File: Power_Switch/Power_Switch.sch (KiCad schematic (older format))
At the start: 13 parts, among them J1 CONN_01X04_MALE, Q1 CSD16570Q5B, Q2 Q_NMOS_GSD, U1 MIC5060, U2 FAN4010

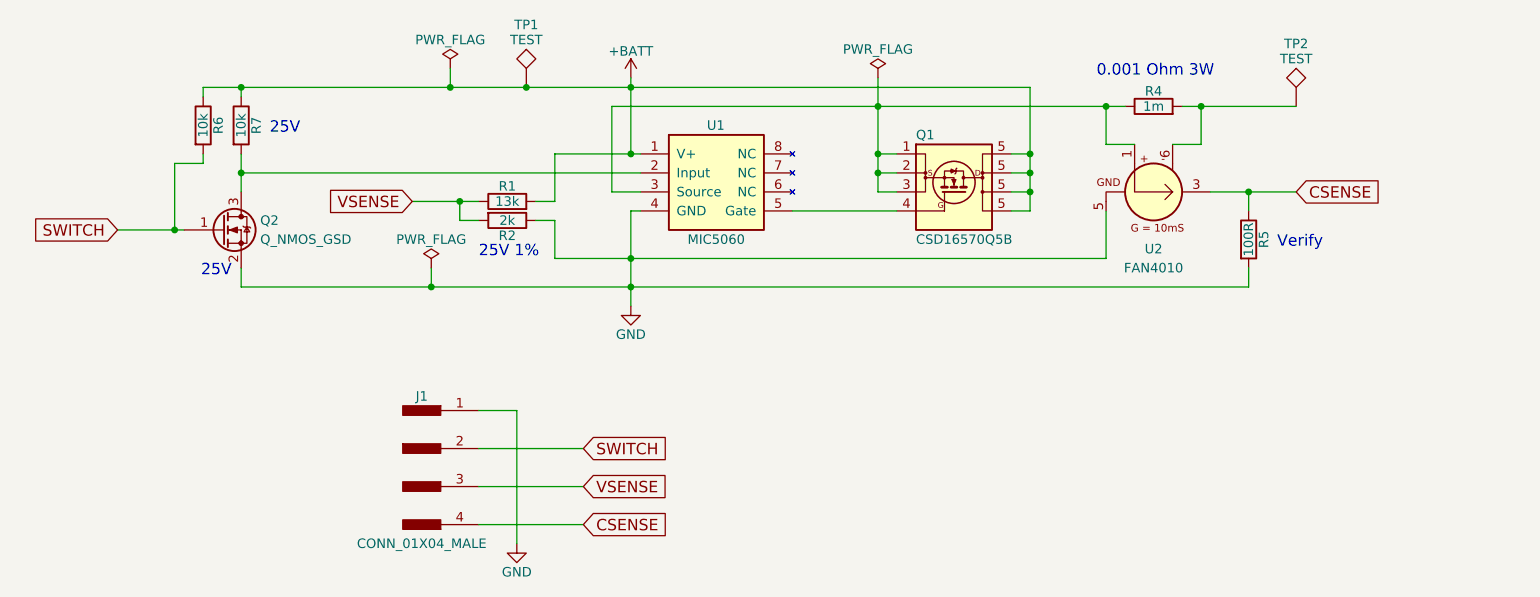
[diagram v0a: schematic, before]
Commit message: Updates GPS Diamond to 1.1.
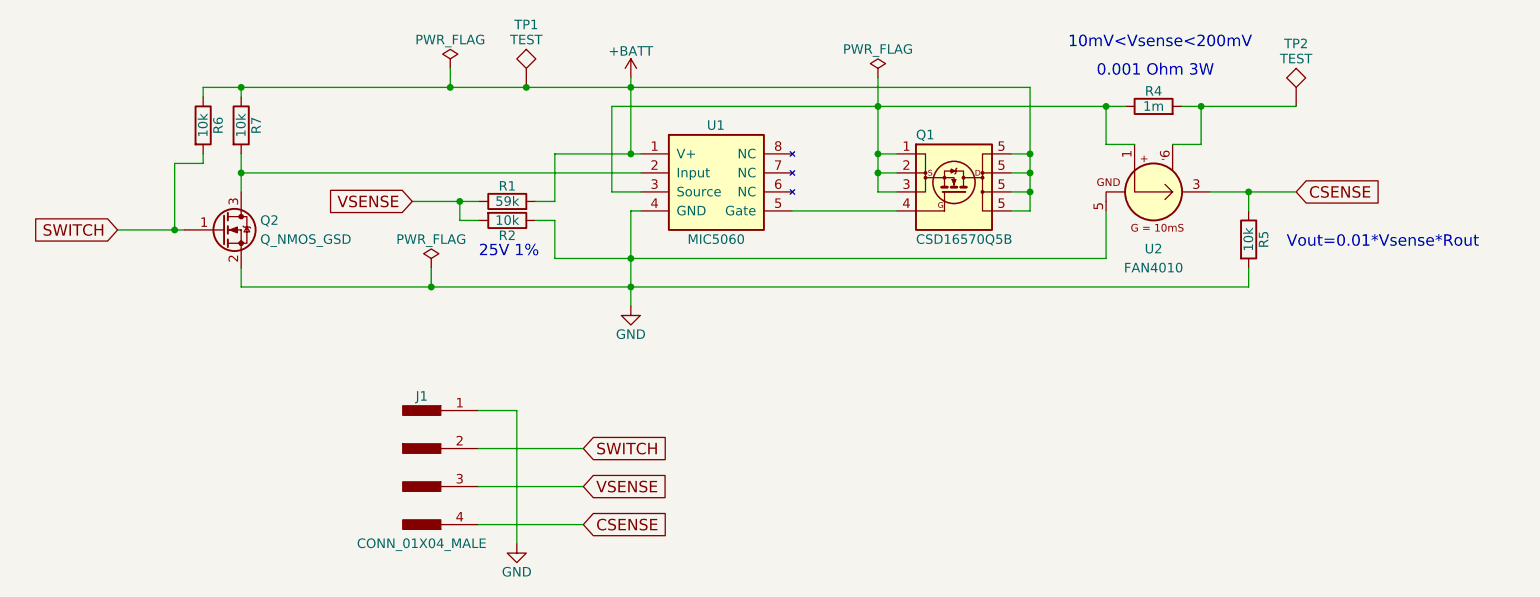
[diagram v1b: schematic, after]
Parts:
- R1: value 13k -> 59k
- R2: value 2k -> 10k
- R5: value 100R -> 10k
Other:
- note added: "10mV<Vsense<200mV"
- note added: "Vout=0.01*Vsense*Rout"
- note removed: "25V"
- note removed: "Verify"
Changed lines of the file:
@@
 P 7100 4200
 F 0 "R5" V 7180 4200 50  0000 C CNN
-F 1 "100R" V 7100 4200 50  0000 C CNN
+F 1 "10k" V 7100 4200 50  0000 C CNN
 F 2 "Resistors_SMD:R_0402" V 7030 4200 50  0001 C CNN
 F 3 "" H 7100 4200 50  0001 C CNN
@@
 P 3200 4000
 F 0 "R1" V 3280 4000 50  0000 C CNN
-F 1 "13k" V 3200 4000 50  0000 C CNN
+F 1 "59k" V 3200 4000 50  0000 C CNN
 F 2 "Resistors_SMD:R_0402" V 3130 4000 50  0001 C CNN
 F 3 "" H 3200 4000 50  0001 C CNN
@@
 P 3200 4100
 F 0 "R2" V 3280 4100 50  0000 C CNN
-F 1 "2k" V 3200 4100 50  0000 C CNN
+F 1 "10k" V 3200 4100 50  0000 C CNN
 F 2 "Resistors_SMD:R_0402" V 3130 4100 50  0001 C CNN
 F 3 "" H 3200 4100 50  0001 C CNN
@@
 Text Notes 3050 4300 0    60   ~ 0
 25V 1%
-Text Notes 7250 4250 0    60   ~ 0
-Verify
 $Comp
 L TEST TP1
@@
 Wire Wire Line
 	1150 4150 1500 4150
-Text Notes 1950 3650 0    60   ~ 0
-25V
 Wire Wire Line
 	1800 4450 1800 4350
@@
 	1600 3450 1600 3400
 Connection ~ 1800 3400
-Text Notes 1750 4400 2    60   ~ 0
-25V
 $Comp
 L Q_NMOS_GSD Q2
@@
 	1    0    0    -1
 $EndComp
+Text Notes 7300 4250 0    60   ~ 0
+Vout=0.01*Vsense*Rout
+Text Notes 6150 3200 0    60   ~ 0
+10mV<Vsense<200mV
 $EndSCHEMATC
